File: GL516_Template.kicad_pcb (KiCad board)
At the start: 2 copper layers, 315.8 x 99.2 mm, 58 parts, among them SW10 SW_PUSH, SW11 SW_PUSH, SW13 SW_PUSH, SW14 SW_PUSH, SW15 SW_PUSH, SW16 SW_PUSH, SW18 SW_PUSH, SW19 SW_PUSH, SW2 KEY_SWITCH, SW20 SW_PUSH, SW23 SW_PUSH, SW24 SW_PUSH, SW25 SW_PUSH, SW27 SW_PUSH, SW28 SW_PUSH, SW29 SW_PUSH, SW30 SW_PUSH, SW32 SW_PUSH, SW33 SW_PUSH, SW34 SW_PUSH, SW35 SW_PUSH, SW37 SW_PUSH, SW38 SW_PUSH, SW39 SW_PUSH, SW4 SW_PUSH, SW42 SW_PUSH, SW43 SW_PUSH, SW44 SW_PUSH, SW46 SW_PUSH, SW47 SW_PUSH, SW48 SW_PUSH, SW49 SW_PUSH, SW5 SW_PUSH, SW51 SW_PUSH, SW52 SW_PUSH, SW53 SW_PUSH, SW54 SW_PUSH, SW56 SW_PUSH, SW57 SW_PUSH, SW58 SW_PUSH, SW59 SW_PUSH, SW6 SW_PUSH, SW61 SW_PUSH, SW62 SW_PUSH, SW63 SW_PUSH, SW64 SW_PUSH, SW7 SW_PUSH

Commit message: 実装プレートの外形線を0.5mm内側へ
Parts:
- removed Ref** (x6): Val**, kbd:HOLE_m2_a
- removed SW13, SW14, SW15, SW16, SW18, SW19, SW20, SW23, SW24, SW25, SW27, SW28, SW29, SW30, SW32, SW33, SW34, SW37, SW38, SW39, SW42, SW43, SW44, SW46, SW47, SW48, SW51 (x2), SW52, SW53 (x3), SW54, SW56, SW57, SW58, SW59, SW63, SW64: SW_PUSH, kbd:SW_Hole
- removed SW35, SW62: SW_PUSH, kbd:SW_Hole_2.25u
- removed SW49: SW_PUSH, kbd:SW_Hole_1.25
- removed SW61: SW_PUSH, kbd:SW_Hole_1.5
- added J10: Conn_01x01, kbd:HOLE_m2_Outline_Fab, F.Cu at (11.1, 120.2)
- added J11: Conn_01x01, kbd:HOLE_m2_Outline_Fab, F.Cu at (108.6, 13.1)
- added J12: Conn_01x01, kbd:HOLE_m2_Outline_Fab, F.Cu at (234.3, 13.1)
- added J13: Conn_01x01, kbd:HOLE_m2_Outline_Fab, F.Cu at (108.6, 120.2)
- added J14: Conn_01x01, kbd:HOLE_m2_Outline_Fab, F.Cu at (234.3, 120.2)
- added J15: Conn_01x01, kbd:HOLE_m2_Outline_Fab, F.Cu at (331.8, 13.1)
- added J16: Conn_01x01, kbd:HOLE_m2_Outline_Fab, F.Cu at (331.8, 66.7)
- added J17: Conn_01x01, kbd:HOLE_m2_Outline_Fab, F.Cu at (331.8, 120.2)
- added J2: Conn_01x01, kbd:HOLE_m2_Outline, F.Cu at (16.1, 21.6)
- added J3: Conn_01x01, kbd:HOLE_m2_Outline, F.Cu at (16.1, 66.7)
- added J4: Conn_01x01, kbd:HOLE_m2_Outline, F.Cu at (16.1, 111.8)
- added J5: Conn_01x01, kbd:HOLE_m2_Outline, F.Cu at (326.8, 21.6)
- added J6: Conn_01x01, kbd:HOLE_m2_Outline, F.Cu at (326.8, 66.7)
- added J7: Conn_01x01, kbd:HOLE_m2_Outline, F.Cu at (326.8, 111.8)
- added J8: Conn_01x01, kbd:HOLE_m2_Outline_Fab, F.Cu at (11.1, 13.1)
- added J9: Conn_01x01, kbd:HOLE_m2_Outline_Fab, F.Cu at (11.1, 66.7)
- added SW4: SW_PUSH, kbd:SW_Hole, F.Cu at (276.2, 28.6)
- added SW4: SW_PUSH, kbd:SW_Hole, F.Cu at (233.4, 66.7)
- added SW4: SW_PUSH, kbd:SW_Hole, F.Cu at (238.1, 28.6)
- added SW4: SW_PUSH, kbd:SW_Hole, F.Cu at (214.3, 66.7)
- added SW4: SW_PUSH, kbd:SW_Hole, F.Cu at (161.9, 28.6)
- added SW4: SW_PUSH, kbd:SW_Hole, F.Cu at (176.2, 66.7)
- added SW4: SW_PUSH, kbd:SW_Hole, F.Cu at (181.0, 28.6)
- added SW4: SW_PUSH, kbd:SW_Hole, F.Cu at (200.0, 28.6)
- added SW4: SW_PUSH, kbd:SW_Hole, F.Cu at (195.3, 66.7)
- added SW4: SW_PUSH, kbd:SW_Hole, F.Cu at (142.9, 28.6)
- added SW4: SW_PUSH, kbd:SW_Hole, F.Cu at (138.1, 66.7)
- added SW4: SW_PUSH, kbd:SW_Hole, F.Cu at (295.3, 28.6)
- added SW4: SW_PUSH, kbd:SW_Hole, F.Cu at (123.8, 28.6)
- added SW4: SW_PUSH, kbd:SW_Hole, F.Cu at (157.2, 66.7)
- added SW4: SW_PUSH, kbd:SW_Hole, F.Cu at (119.1, 66.7)
- added SW4: SW_PUSH, kbd:SW_Hole, F.Cu at (104.8, 28.6)
- added SW4: SW_PUSH, kbd:SW_Hole, F.Cu at (100.0, 66.7)
- added SW4: SW_PUSH, kbd:SW_Hole, F.Cu at (85.7, 28.6)
- added SW4: SW_PUSH, kbd:SW_Hole, F.Cu at (81.0, 66.7)
- added SW4: SW_PUSH, kbd:SW_Hole, F.Cu at (66.7, 28.6)
- added SW4: SW_PUSH, kbd:SW_Hole, F.Cu at (61.9, 66.7)
- added SW4: KEY_SWITCH, kbd:SW_Hole_2u, F.Cu at (38.1, 85.7)
- added SW4: SW_PUSH, kbd:SW_Hole, F.Cu at (314.3, 66.7)
- added SW4: SW_PUSH, kbd:SW_Hole, F.Cu at (314.3, 28.6)
- added SW4: KEY_SWITCH, kbd:SW_Hole_2u, F.Cu at (292.9, 57.1)
- added SW4: SW_PUSH, kbd:SW_Hole, F.Cu at (252.4, 66.7)
- added SW4: SW_PUSH, kbd:SW_Hole, F.Cu at (219.1, 28.6)
- added SW4: SW_PUSH, kbd:SW_Hole, F.Cu at (257.2, 28.6)
- added SW4: SW_PUSH, kbd:SW_Hole, F.Cu at (271.5, 66.7)
- added SW5: SW_PUSH, kbd:SW_Hole_1.25, F.Cu at (226.2, 104.8)
- added SW5: SW_PUSH, kbd:SW_Hole_1.25, F.Cu at (202.4, 104.8)
- added SW5: SW_PUSH, kbd:SW_Hole_1.25, F.Cu at (178.6, 104.8)
- added SW8: SW_PUSH, kbd:SW_Hole, F.Cu at (247.7, 104.8)
- added SW8: SW_PUSH, kbd:SW_Hole, F.Cu at (266.7, 47.6)
- added SW8: SW_PUSH, kbd:SW_Hole, F.Cu at (247.7, 47.6)
- added SW8: SW_PUSH, kbd:SW_Hole, F.Cu at (228.6, 47.6)
- added SW8: SW_PUSH, kbd:SW_Hole, F.Cu at (238.1, 85.7)
- added SW8: SW_PUSH, kbd:SW_Hole, F.Cu at (257.2, 85.7)
- added SW8: SW_PUSH, kbd:SW_Hole, F.Cu at (276.2, 85.7)
- added SW8: SW_PUSH, kbd:SW_Hole, F.Cu at (190.5, 47.6)
- added SW8: SW_PUSH, kbd:SW_Hole, F.Cu at (171.4, 47.6)
- added SW8: SW_PUSH, kbd:SW_Hole, F.Cu at (200.0, 85.7)
- added SW8: SW_PUSH, kbd:SW_Hole, F.Cu at (219.1, 85.7)
- added SW8: SW_PUSH, kbd:SW_Hole, F.Cu at (138.1, 104.8)
- added SW8: SW_PUSH, kbd:SW_Hole, F.Cu at (209.6, 47.6)
- added SW8: SW_PUSH, kbd:SW_Hole, F.Cu at (181.0, 85.7)
- added SW8: SW_PUSH, kbd:SW_Hole, F.Cu at (123.8, 85.7)
- added SW8: SW_PUSH, kbd:SW_Hole, F.Cu at (152.4, 47.6)
- added SW8: SW_PUSH, kbd:SW_Hole, F.Cu at (142.9, 85.7)
- added SW8: SW_PUSH, kbd:SW_Hole, F.Cu at (133.3, 47.6)
- added SW8: SW_PUSH, kbd:SW_Hole, F.Cu at (161.9, 85.7)
- added SW8: SW_PUSH, kbd:SW_Hole, F.Cu at (114.3, 47.6)
- added SW8: SW_PUSH, kbd:SW_Hole, F.Cu at (95.2, 104.8)
- added SW8: SW_PUSH, kbd:SW_Hole, F.Cu at (104.8, 85.7)
- added SW8: SW_PUSH, kbd:SW_Hole, F.Cu at (157.2, 104.8)
- added SW8: SW_PUSH, kbd:SW_Hole, F.Cu at (95.2, 47.6)
- added SW8: SW_PUSH, kbd:SW_Hole, F.Cu at (85.7, 85.7)
- added SW8: SW_PUSH, kbd:SW_Hole, F.Cu at (76.2, 47.6)
- added SW8: SW_PUSH, kbd:SW_Hole, F.Cu at (66.7, 85.7)
- added SW8: SW_PUSH, kbd:SW_Hole, F.Cu at (295.3, 104.8)
- added SW8: SW_PUSH, kbd:SW_Hole, F.Cu at (314.3, 104.8)
- added SW8: SW_PUSH, kbd:SW_Hole, F.Cu at (276.2, 104.8)
- added SW8: SW_PUSH, kbd:SW_Hole, F.Cu at (295.3, 85.7)
- added SW8: SW_PUSH, kbd:SW_Hole, F.Cu at (314.3, 47.6)
- added SW8: SW_PUSH, kbd:SW_Hole, F.Cu at (314.3, 85.7)
- SW2: footprint kbd:SW_Hole_2u -> kbd:SW_Hole_1.5
- moved SW5 97.2 mm to (116.7, 104.8)
- moved SW2 88.5 mm to (33.3, 47.6), turned to 0 degrees
- moved SW7 53.3 mm to (52.4, 104.8)
- moved SW7 24.3 mm to (73.8, 104.8)
- moved SW8 23.5 mm to (57.1, 47.6)
- moved SW7 15.1 mm to (31.0, 104.8)
- moved SW4 8.73 mm to (47.6, 28.6)
- moved SW1 8.73 mm to (28.6, 28.6)
- moved SW3 4.00 mm to (35.7, 66.7)
- renumbered SW4 to SW1, SW6 to SW3, SW10 to SW7, SW11 to SW8

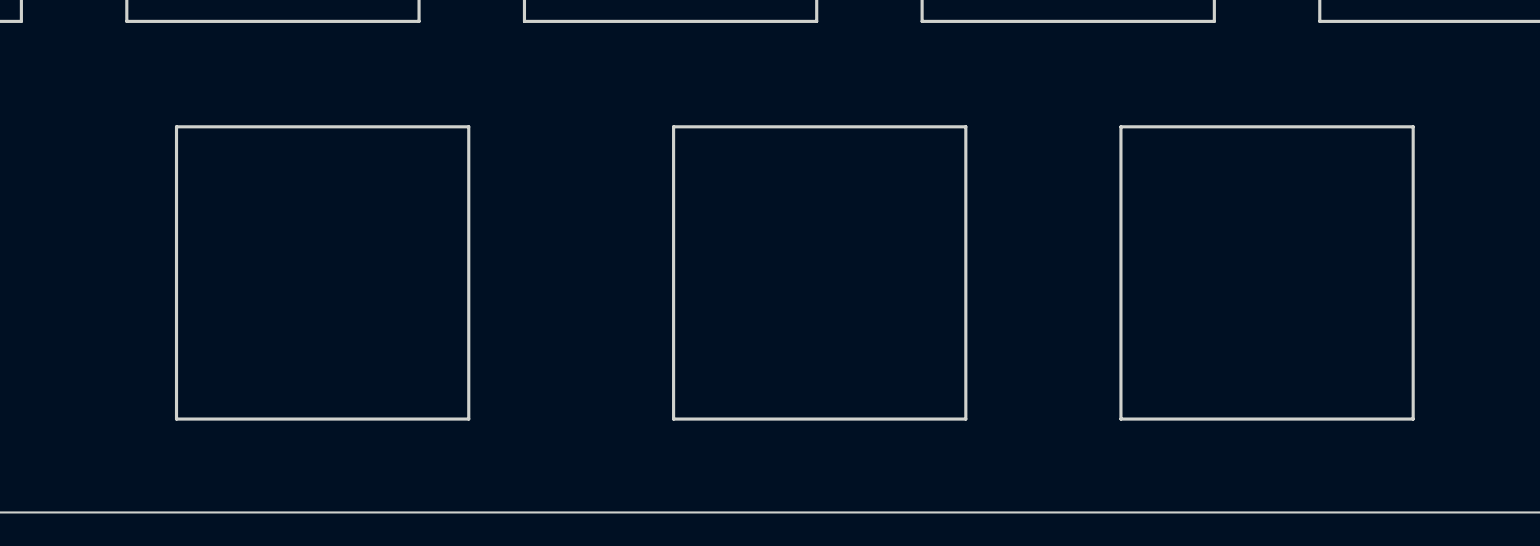
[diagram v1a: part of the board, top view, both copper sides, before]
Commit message: LED回路図更新
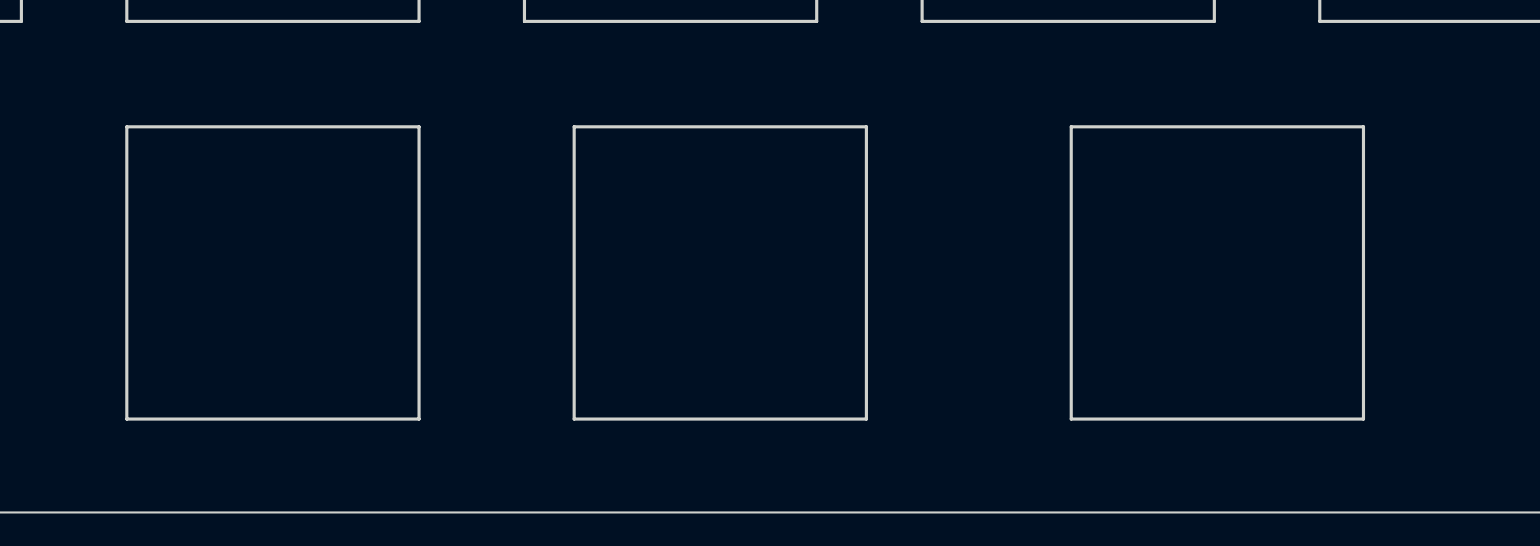
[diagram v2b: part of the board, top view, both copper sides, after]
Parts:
- moved SW8 47.6 mm to (200.0, 104.8)
- moved SW5 19.1 mm to (245.3, 104.8)
- moved SW5 19.1 mm to (221.5, 104.8)
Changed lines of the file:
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@@
   )
   (module kbd:SW_Hole (layer F.Cu)
-    (at 247.65 104.775)
+    (at 200.025 104.775)
     (fp_text reference SW8 (at 7 8.1) (layer F.SilkS) hide
       (effects (font (size 1 1) (thickness 0.15)))
@@
   )
   (module kbd:SW_Hole_1.25 (layer F.Cu)
-    (at 226.21875 104.775)
+    (at 245.26875 104.775)
     (fp_text reference SW5 (at 7 8.1) (layer F.SilkS) hide
       (effects (font (size 1 1) (thickness 0.15)))
@@
   )
   (module kbd:SW_Hole_1.25 (layer F.Cu)
-    (at 202.40625 104.775)
+    (at 221.45625 104.775)
     (fp_text reference SW5 (at 7 8.1) (layer F.SilkS) hide
       (effects (font (size 1 1) (thickness 0.15)))

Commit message: フットプリントを更新
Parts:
- J10, J11, J12, J13, J14, J15, J16, J17, J8, J9: footprint kbd:HOLE_m2_Outline_Fab -> kbd_Hole:m2_Screw_Hole_Fab
- J2, J3, J4, J5, J6, J7: footprint kbd:HOLE_m2_Outline -> kbd_Hole:m2_Screw_Hole_EdgeCuts
- SW1, SW4 (x28), SW7, SW8 (x34): footprint kbd:SW_Hole -> kbd_SW_Hole:SW_Hole
- SW2: footprint kbd:SW_Hole_1.5 -> kbd_SW_Hole:SW_Hole_1.5
- SW3: footprint kbd:SW_Hole_1.75 -> kbd_SW_Hole:SW_Hole_1.75
- SW4 (x2): footprint kbd:SW_Hole_2u -> kbd_SW_Hole:SW_Hole_2u
- SW5 (x4), SW7 (x2): footprint kbd:SW_Hole_1.25 -> kbd_SW_Hole:SW_Hole_1.25

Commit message: 基板サイズ微修正
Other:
- board size 315.8 x 99.2 mm -> 315.4 x 99.2 mm
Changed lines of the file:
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@@
   (general
     (thickness 1.6)
-    (drawings 44)
+    (drawings 46)
     (tracks 0)
     (zones 0)
@@
   )
   (setup
-    (last_trace_width 0.5)
+    (last_trace_width 0.25)
     (user_trace_width 0.5)
     (user_trace_width 0.5)
@@
     (fp_line (start 9.525 9.525) (end 9.525 -9.525) (layer F.Fab) (width 0.15))
   )
+  (gr_line (start 13.575 113.75) (end 13.575 19.55) (layer F.Fab) (width 0.15))
+  (gr_line (start 329.325 19.55) (end 329.325 113.75) (layer F.Fab) (width 0.15))
   (gr_line (start 10.075 122.75) (end 8.575 121.25) (layer F.Fab) (width 0.15))
   (gr_line (start 334.325 12.05) (end 332.825 10.55) (layer F.Fab) (width 0.15))
@@
   (gr_line (start 78.575 20.55) (end 264.325 20.55) (layer F.Fab) (width 0.15))
   (gr_line (start 10.45 50.55) (end 332.4 50.55) (layer F.Fab) (width 0.15))
-  (gr_arc (start 320.825 20.05) (end 323.825 20.05) (angle -90) (layer F.Fab) (width 0.1))
-  (gr_arc (start 320.825 113.25) (end 320.825 116.25) (angle -90) (layer F.Fab) (width 0.1))
-  (gr_arc (start 22.075 20.05) (end 22.075 17.05) (angle -90) (layer F.Fab) (width 0.1))
-  (gr_arc (start 22.075 113.25) (end 19.075 113.25) (angle -90) (layer F.Fab) (width 0.1))
+  (gr_arc (start 320.625 20.05) (end 323.625 20.05) (angle -90) (layer F.Fab) (width 0.1))
+  (gr_arc (start 320.625 113.25) (end 320.625 116.25) (angle -90) (layer F.Fab) (width 0.1))
+  (gr_arc (start 22.275 20.05) (end 22.275 17.05) (angle -90) (layer F.Fab) (width 0.1))
+  (gr_arc (start 22.275 113.25) (end 19.275 113.25) (angle -90) (layer F.Fab) (width 0.1))
   (gr_text "Do not place switches to the left of this line." (at 32.5 13.7) (layer F.Fab)
     (effects (font (size 1 1) (thickness 0.15)))
@@
     (effects (font (size 1 1) (thickness 0.15)))
   )
-  (gr_line (start 323.825 20.05) (end 323.825 113.25) (layer F.Fab) (width 0.1))
-  (gr_line (start 19.075 20.05) (end 19.075 113.25) (layer F.Fab) (width 0.1))
-  (gr_arc (start 16.575 113.25) (end 13.575 113.25) (angle -90) (layer Edge.Cuts) (width 0.1))
-  (gr_arc (start 16.575 20.05) (end 16.575 17.05) (angle -90) (layer Edge.Cuts) (width 0.1))
-  (gr_arc (start 326.325 20.05) (end 329.325 20.05) (angle -90) (layer Edge.Cuts) (width 0.1))
-  (gr_arc (start 326.325 113.25) (end 326.325 116.25) (angle -90) (layer Edge.Cuts) (width 0.1))
-  (gr_line (start 329.325 113.25) (end 329.325 20.05) (layer Edge.Cuts) (width 0.1))
-  (gr_line (start 16.575 116.25) (end 326.325 116.25) (layer Edge.Cuts) (width 0.1))
-  (gr_line (start 13.575 20.05) (end 13.575 113.25) (layer Edge.Cuts) (width 0.1))
-  (gr_line (start 326.325 17.05) (end 16.575 17.05) (layer Edge.Cuts) (width 0.1))
+  (gr_line (start 323.625 20.05) (end 323.625 113.25) (layer F.Fab) (width 0.1))
+  (gr_line (start 19.275 20.05) (end 19.275 113.25) (layer F.Fab) (width 0.1))
+  (gr_arc (start 16.775 113.25) (end 13.775 113.25) (angle -90) (layer Edge.Cuts) (width 0.1))
+  (gr_arc (start 16.775 20.05) (end 16.775 17.05) (angle -90) (layer Edge.Cuts) (width 0.1))
+  (gr_arc (start 326.125 20.05) (end 329.125 20.05) (angle -90) (layer Edge.Cuts) (width 0.1))
+  (gr_arc (start 326.125 113.25) (end 326.125 116.25) (angle -90) (layer Edge.Cuts) (width 0.1))
+  (gr_line (start 329.125 113.25) (end 329.125 20.05) (layer Edge.Cuts) (width 0.1))
+  (gr_line (start 16.775 116.25) (end 326.125 116.25) (layer Edge.Cuts) (width 0.1))
+  (gr_line (start 13.775 20.05) (end 13.775 113.25) (layer Edge.Cuts) (width 0.1))
+  (gr_line (start 326.125 17.05) (end 16.775 17.05) (layer Edge.Cuts) (width 0.1))
 )

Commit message: 寸法変更
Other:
- board size 315.4 x 99.2 mm -> 314.4 x 99.2 mm
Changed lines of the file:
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@@
   (general
     (thickness 1.6)
-    (drawings 46)
+    (drawings 48)
     (tracks 0)
     (zones 0)
@@
     (fp_line (start 9.525 9.525) (end 9.525 -9.525) (layer F.Fab) (width 0.15))
   )
+  (dimension 314.35 (width 0.15) (layer F.Fab)
+    (gr_text "314.350 mm" (at 171.45 -1.3) (layer F.Fab)
+      (effects (font (size 1 1) (thickness 0.15)))
+    )
+    (feature1 (pts (xy 328.625 20.05) (xy 328.625 -0.586421)))
+    (feature2 (pts (xy 14.275 20.05) (xy 14.275 -0.586421)))
+    (crossbar (pts (xy 14.275 0) (xy 328.625 0)))
+    (arrow1a (pts (xy 328.625 0) (xy 327.498496 0.586421)))
+    (arrow1b (pts (xy 328.625 0) (xy 327.498496 -0.586421)))
+    (arrow2a (pts (xy 14.275 0) (xy 15.401504 0.586421)))
+    (arrow2b (pts (xy 14.275 0) (xy 15.401504 -0.586421)))
+  )
+  (dimension 304.35 (width 0.15) (layer F.Fab)
+    (gr_text "304.350 mm" (at 171.45 5.84375) (layer F.Fab)
+      (effects (font (size 1 1) (thickness 0.15)))
+    )
+    (feature1 (pts (xy 19.275 20.05) (xy 19.275 6.557329)))
+    (feature2 (pts (xy 323.625 20.05) (xy 323.625 6.557329)))
+    (crossbar (pts (xy 323.625 7.14375) (xy 19.275 7.14375)))
+    (arrow1a (pts (xy 19.275 7.14375) (xy 20.401504 6.557329)))
+    (arrow1b (pts (xy 19.275 7.14375) (xy 20.401504 7.730171)))
+    (arrow2a (pts (xy 323.625 7.14375) (xy 322.498496 6.557329)))
+    (arrow2b (pts (xy 323.625 7.14375) (xy 322.498496 7.730171)))
+  )
   (gr_line (start 13.575 113.75) (end 13.575 19.55) (layer F.Fab) (width 0.15))
   (gr_line (start 329.325 19.55) (end 329.325 113.75) (layer F.Fab) (width 0.15))
@@
   (gr_line (start 323.625 20.05) (end 323.625 113.25) (layer F.Fab) (width 0.1))
   (gr_line (start 19.275 20.05) (end 19.275 113.25) (layer F.Fab) (width 0.1))
-  (gr_arc (start 16.775 113.25) (end 13.775 113.25) (angle -90) (layer Edge.Cuts) (width 0.1))
-  (gr_arc (start 16.775 20.05) (end 16.775 17.05) (angle -90) (layer Edge.Cuts) (width 0.1))
-  (gr_arc (start 326.125 20.05) (end 329.125 20.05) (angle -90) (layer Edge.Cuts) (width 0.1))
-  (gr_arc (start 326.125 113.25) (end 326.125 116.25) (angle -90) (layer Edge.Cuts) (width 0.1))
-  (gr_line (start 329.125 113.25) (end 329.125 20.05) (layer Edge.Cuts) (width 0.1))
-  (gr_line (start 16.775 116.25) (end 326.125 116.25) (layer Edge.Cuts) (width 0.1))
-  (gr_line (start 13.775 20.05) (end 13.775 113.25) (layer Edge.Cuts) (width 0.1))
-  (gr_line (start 326.125 17.05) (end 16.775 17.05) (layer Edge.Cuts) (width 0.1))
+  (gr_arc (start 17.275 113.25) (end 14.275 113.25) (angle -90) (layer Edge.Cuts) (width 0.1))
+  (gr_arc (start 17.275 20.05) (end 17.275 17.05) (angle -90) (layer Edge.Cuts) (width 0.1))
+  (gr_arc (start 325.625 20.05) (end 328.625 20.05) (angle -90) (layer Edge.Cuts) (width 0.1))
+  (gr_arc (start 325.625 113.25) (end 325.625 116.25) (angle -90) (layer Edge.Cuts) (width 0.1))
+  (gr_line (start 328.625 113.25) (end 328.625 20.05) (layer Edge.Cuts) (width 0.1))
+  (gr_line (start 17.275 116.25) (end 325.625 116.25) (layer Edge.Cuts) (width 0.1))
+  (gr_line (start 14.275 20.05) (end 14.275 113.25) (layer Edge.Cuts) (width 0.1))
+  (gr_line (start 325.625 17.05) (end 17.275 17.05) (layer Edge.Cuts) (width 0.1))
 )

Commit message: 寸法更新
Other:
- board size 314.4 x 99.2 mm -> 314.4 x 98.8 mm
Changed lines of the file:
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@@
   (gr_line (start 78.575 20.55) (end 264.325 20.55) (layer F.Fab) (width 0.15))
   (gr_line (start 10.45 50.55) (end 332.4 50.55) (layer F.Fab) (width 0.15))
-  (gr_arc (start 320.625 20.05) (end 323.625 20.05) (angle -90) (layer F.Fab) (width 0.1))
-  (gr_arc (start 320.625 113.25) (end 320.625 116.25) (angle -90) (layer F.Fab) (width 0.1))
-  (gr_arc (start 22.275 20.05) (end 22.275 17.05) (angle -90) (layer F.Fab) (width 0.1))
-  (gr_arc (start 22.275 113.25) (end 19.275 113.25) (angle -90) (layer F.Fab) (width 0.1))
+  (gr_arc (start 320.625 20.25) (end 323.625 20.25) (angle -90) (layer F.Fab) (width 0.1))
+  (gr_arc (start 320.625 113.05) (end 320.625 116.05) (angle -90) (layer F.Fab) (width 0.1))
+  (gr_arc (start 22.275 20.25) (end 22.275 17.25) (angle -90) (layer F.Fab) (width 0.1))
+  (gr_arc (start 22.275 113.05) (end 19.275 113.05) (angle -90) (layer F.Fab) (width 0.1))
   (gr_text "Do not place switches to the left of this line." (at 32.5 13.7) (layer F.Fab)
     (effects (font (size 1 1) (thickness 0.15)))
@@
     (effects (font (size 1 1) (thickness 0.15)))
   )
-  (gr_line (start 323.625 20.05) (end 323.625 113.25) (layer F.Fab) (width 0.1))
-  (gr_line (start 19.275 20.05) (end 19.275 113.25) (layer F.Fab) (width 0.1))
-  (gr_arc (start 17.275 113.25) (end 14.275 113.25) (angle -90) (layer Edge.Cuts) (width 0.1))
-  (gr_arc (start 17.275 20.05) (end 17.275 17.05) (angle -90) (layer Edge.Cuts) (width 0.1))
-  (gr_arc (start 325.625 20.05) (end 328.625 20.05) (angle -90) (layer Edge.Cuts) (width 0.1))
-  (gr_arc (start 325.625 113.25) (end 325.625 116.25) (angle -90) (layer Edge.Cuts) (width 0.1))
-  (gr_line (start 328.625 113.25) (end 328.625 20.05) (layer Edge.Cuts) (width 0.1))
-  (gr_line (start 17.275 116.25) (end 325.625 116.25) (layer Edge.Cuts) (width 0.1))
-  (gr_line (start 14.275 20.05) (end 14.275 113.25) (layer Edge.Cuts) (width 0.1))
-  (gr_line (start 325.625 17.05) (end 17.275 17.05) (layer Edge.Cuts) (width 0.1))
+  (gr_line (start 323.625 20.25) (end 323.625 113.05) (layer F.Fab) (width 0.1))
+  (gr_line (start 19.275 20.25) (end 19.275 113.05) (layer F.Fab) (width 0.1))
+  (gr_arc (start 17.275 113.05) (end 14.275 113.05) (angle -90) (layer Edge.Cuts) (width 0.1))
+  (gr_arc (start 17.275 20.25) (end 17.275 17.25) (angle -90) (layer Edge.Cuts) (width 0.1))
+  (gr_arc (start 325.625 20.25) (end 328.625 20.25) (angle -90) (layer Edge.Cuts) (width 0.1))
+  (gr_arc (start 325.625 113.05) (end 325.625 116.05) (angle -90) (layer Edge.Cuts) (width 0.1))
+  (gr_line (start 328.625 113.05) (end 328.625 20.25) (layer Edge.Cuts) (width 0.1))
+  (gr_line (start 17.275 116.05) (end 325.625 116.05) (layer Edge.Cuts) (width 0.1))
+  (gr_line (start 14.275 20.25) (end 14.275 113.05) (layer Edge.Cuts) (width 0.1))
+  (gr_line (start 325.625 17.25) (end 17.275 17.25) (layer Edge.Cuts) (width 0.1))
 )

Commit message: ProMicro使用時のUSBコネクタの向きを記載
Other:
- board text added: "USB connector to the right.▶"
- board text added: "◀USB connector to the left."
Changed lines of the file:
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@@
   (general
     (thickness 1.6)
-    (drawings 48)
+    (drawings 50)
     (tracks 0)
     (zones 0)
@@
     (fp_line (start 9.525 9.525) (end 9.525 -9.525) (layer F.Fab) (width 0.15))
   )
+  (gr_text "◀USB connector to the left." (at 306.61 8.76) (layer F.Fab)
+    (effects (font (size 1.5 1.5) (thickness 0.3)))
+  )
+  (gr_text "USB connector to the right.▶" (at 38.16 8.7) (layer F.Fab)
+    (effects (font (size 1.5 1.5) (thickness 0.3)))
+  )
   (dimension 314.35 (width 0.15) (layer F.Fab)

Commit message: スイッチ穴の寸法を14.1mmに変更
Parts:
- SW1, SW4 (x28), SW7, SW8 (x34): footprint kbd_SW_Hole:SW_Hole -> kbd_SW_Hole:SW_Hole_1
- SW4 (x2): footprint kbd_SW_Hole:SW_Hole_2u -> kbd_SW_Hole:SW_Hole_2
